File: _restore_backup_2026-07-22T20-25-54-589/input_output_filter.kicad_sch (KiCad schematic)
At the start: 39 parts, among them J1 NC3MAH, J2 NC3MAH, J3 NC3MAH, J4 NC3MAH, J5 XLR3_AudioJack3_Combo_Ground, J6 XLR3_AudioJack3_Combo_Ground, SW6 SW_SPST, SW7 SW_SPST, U5 IH0515S

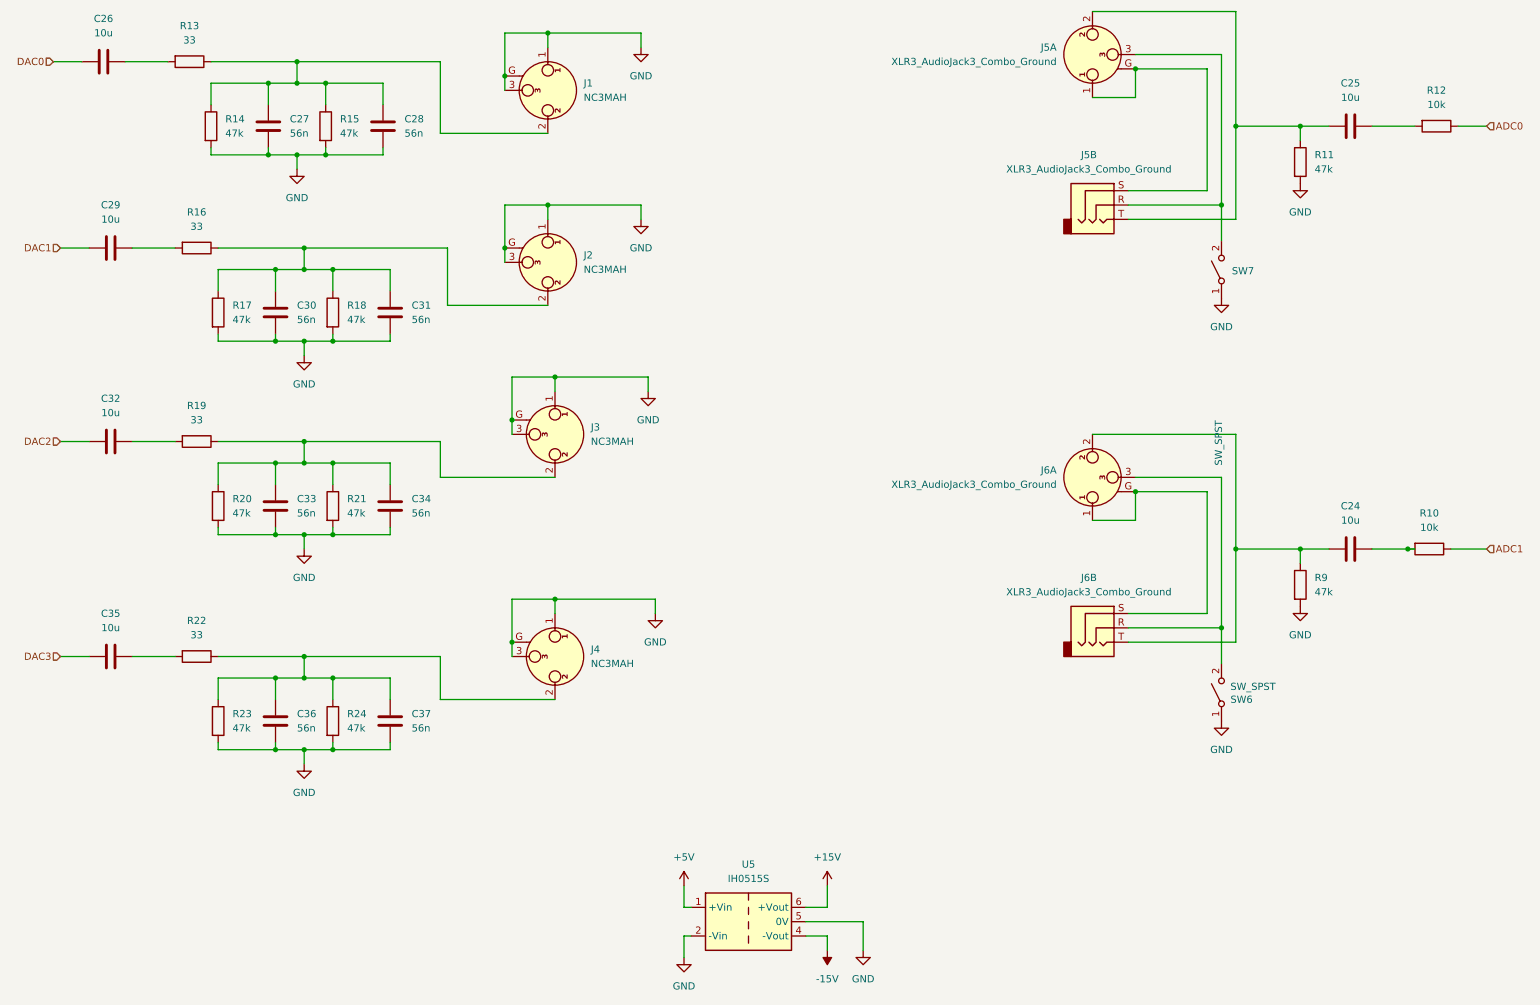
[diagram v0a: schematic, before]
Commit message: aggiunto cad 3d dei connettori
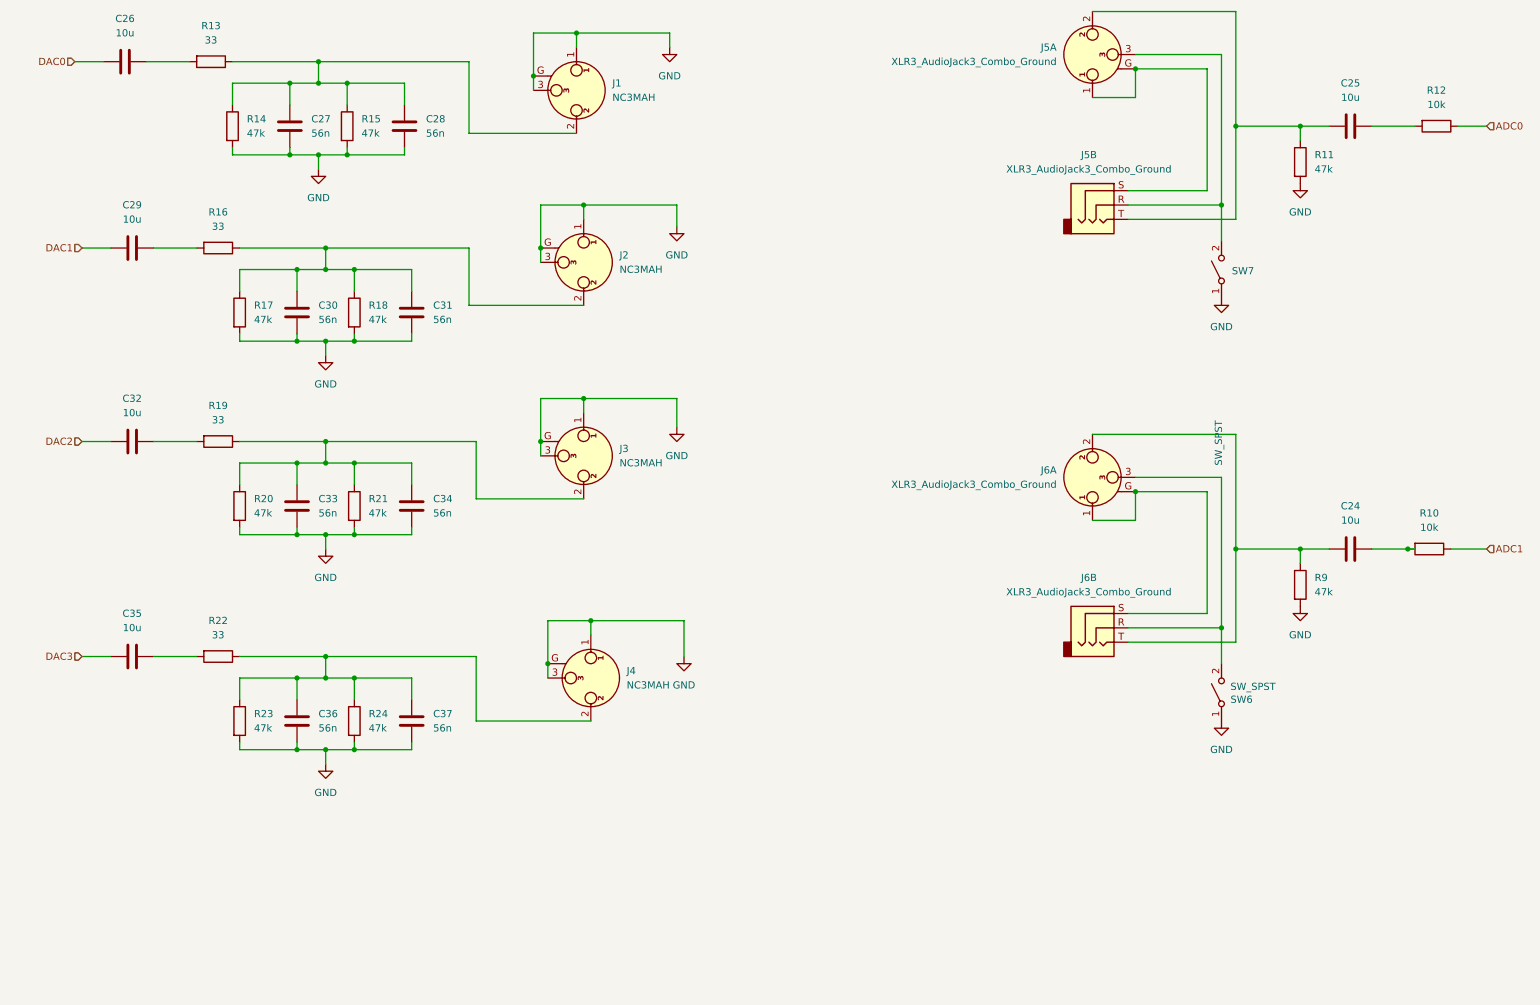
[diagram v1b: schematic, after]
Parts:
- removed U5: IH0515S, Converter_DCDC:Converter_DCDC_XP_POWER-IHxxxxS_THT, symbol Converter_DCDC:IH0515S
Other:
- moved on the sheet: C26, C27, C28, C29, C30, C31, C32, C33, C34, C35, C36, C37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
